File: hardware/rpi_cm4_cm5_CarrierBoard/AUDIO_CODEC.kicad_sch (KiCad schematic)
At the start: 28 parts, among them J13 SJ-3523-SMT-TR, J14 SJ-3523-SMT-TR, U33 SGTL5000XNBA3R2, U34 12MHz, X1 CMM-3729AT-42308-TR

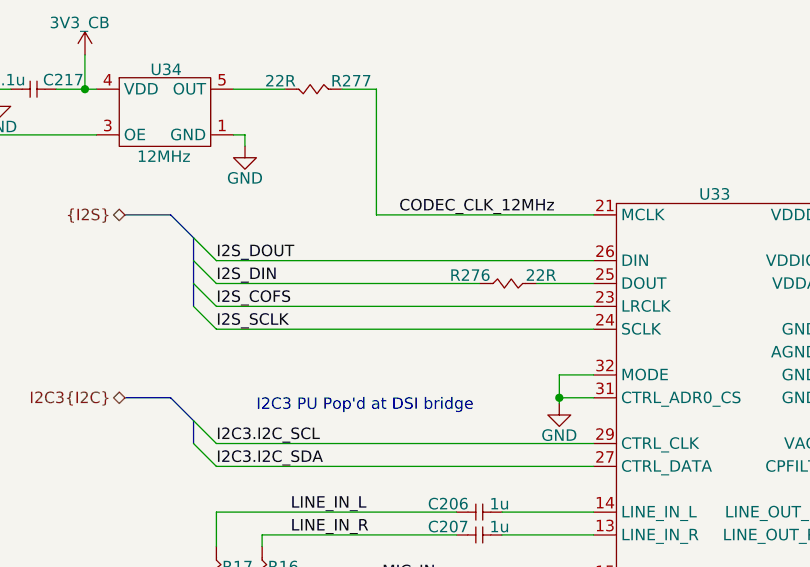
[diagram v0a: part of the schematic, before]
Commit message: Add test points on relevant signals Re-generate SCH_PDF Re-generate BOM Re-generate all gerbers and relevant PCB output files (still in review phase)
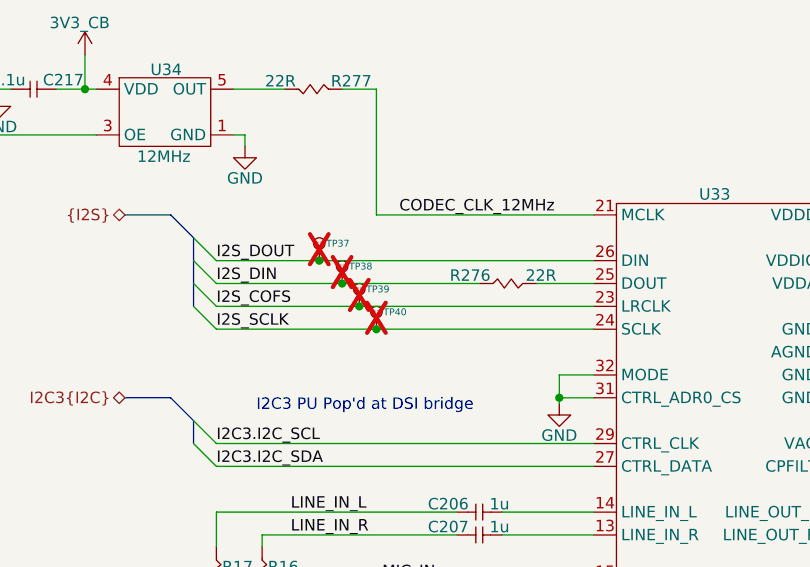
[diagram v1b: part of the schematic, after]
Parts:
- added TP37, TP38, TP39, TP40: 28 mils, footprint:SMT_TP_28_MILS, symbol KicadCompDb:Test Point/TP_00001
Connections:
- net I2S_COFS: now also TP39.1
- net I2S_DIN: now also TP38.1
- net I2S_DOUT: now also TP37.1
- net I2S_SCLK: now also TP40.1

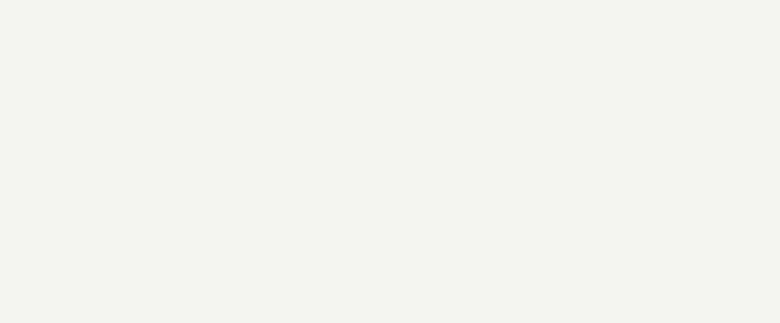
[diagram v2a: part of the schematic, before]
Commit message: Update schematic sheets (assembly variants, default cap / res notes)
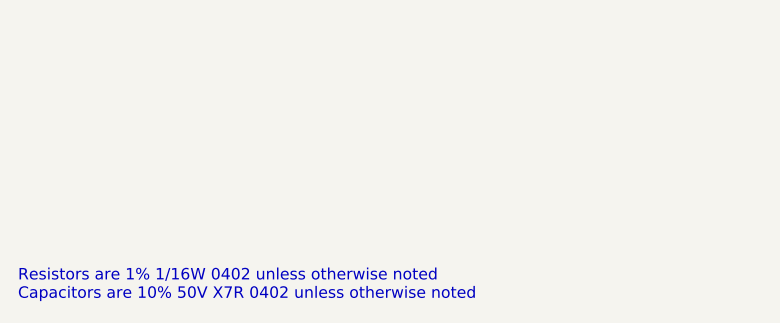
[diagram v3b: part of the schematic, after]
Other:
- note added: "Resistors are 1% 1/16W 0402 unless otherwise noted Capacitors are 10% 50V X7R 0402 unless otherwise noted"
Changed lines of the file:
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@@
 	(title_block
 		(title "RPI CMx Carrier")
-		(date "2026-02-20")
+		(date "2026-02-22")
 		(rev "2.00-0A")
 		(comment 1 "Jean-Francois Bilodeau")
@@
 		(comment 9 "RPI_CMx_Carrier_2.00-0A_BOM")
 	)
+	(text "Resistors are 1% 1/16W 0402 unless otherwise noted\nCapacitors are 10% 50V X7R 0402 unless otherwise noted"
+		(exclude_from_sim no)
+		(at 12.7 170.688 0)
+		(effects
+			(font
+				(size 1.27 1.27)
+			)
+			(justify left)
+		)
+	)
 	(text "I2C3 PU Pop'd at DSI bridge"

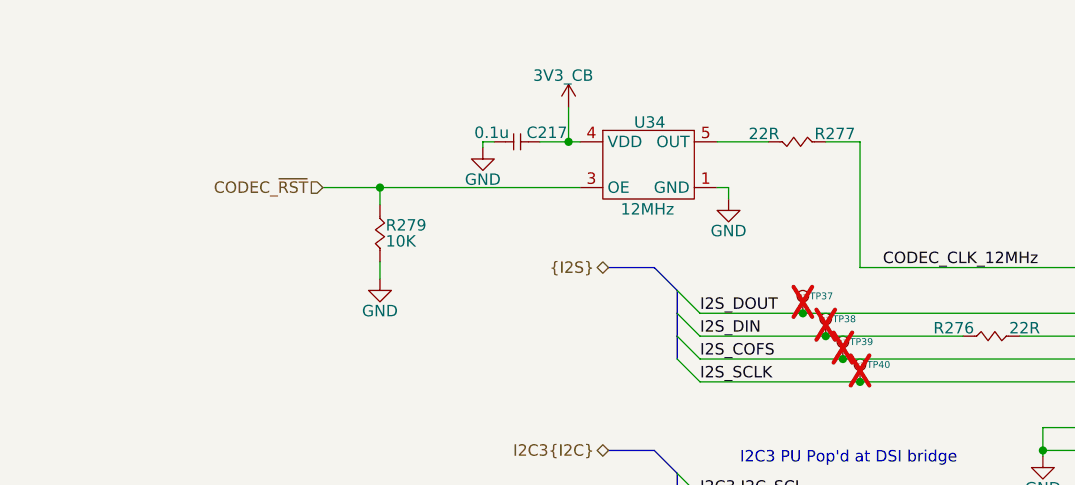
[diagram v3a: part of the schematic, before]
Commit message: Update 12MHz oscillator on Audio Codec schematic sheet to solve single source issue and uncommon packaging. Re-generate all output files including schematics and BOM, as well as all PCB output files
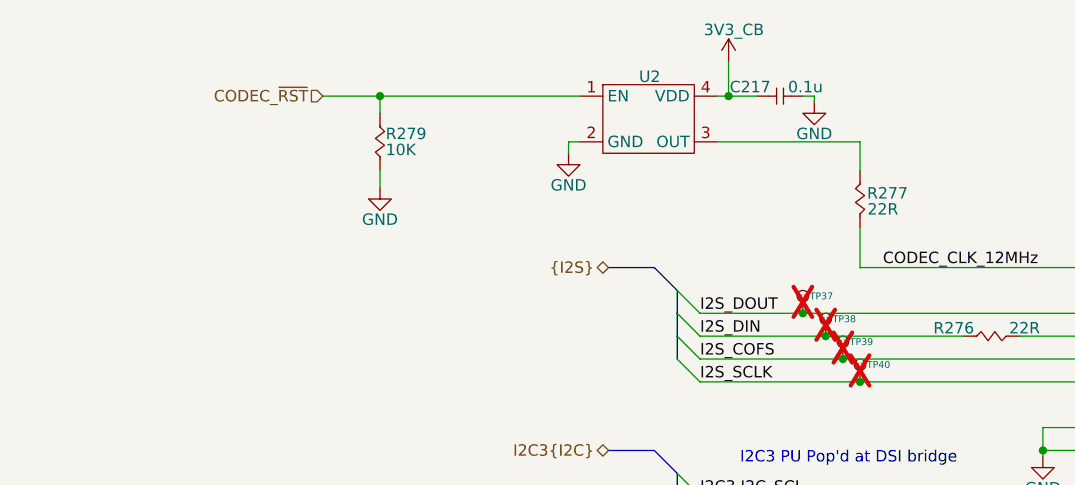
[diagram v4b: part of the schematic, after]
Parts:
- removed U34: 12MHz, footprint:SOT-23-5, symbol KicadCompDb:Oscillator/OSC_00001
- added U2: ECS-2016MVQ-120-BP-TR, footprint:4-SMD_2mmx1_6mm, symbol KicadCompDb:Oscillator/OSC_00003
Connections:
- net 3V3_CB: now also U2.4 (VDD)
- net CODEC_~{RST}: now also U2.1 (EN)
- net GND: now also U2.2 (GND)
- net at R277.1: now also U2.3 (OUT)
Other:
- moved on the sheet: C217, R277, R279
